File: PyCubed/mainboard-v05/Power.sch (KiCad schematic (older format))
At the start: 70 parts, among them J14 Conn_01x06, Q1 IRLML2803, Q2 MBT2222ADW1T1, Q22 NDS8434, Q3 MBT2222ADW1T1, U17 BQ25883RGER, U21 TPS7A4501DCQT, U4 ADM1176-1ARMZ-R7, U5 TPS54226PWPRPWP14_2P31X2P46-L, U6 LTC4121, U7 KF50BD-TR

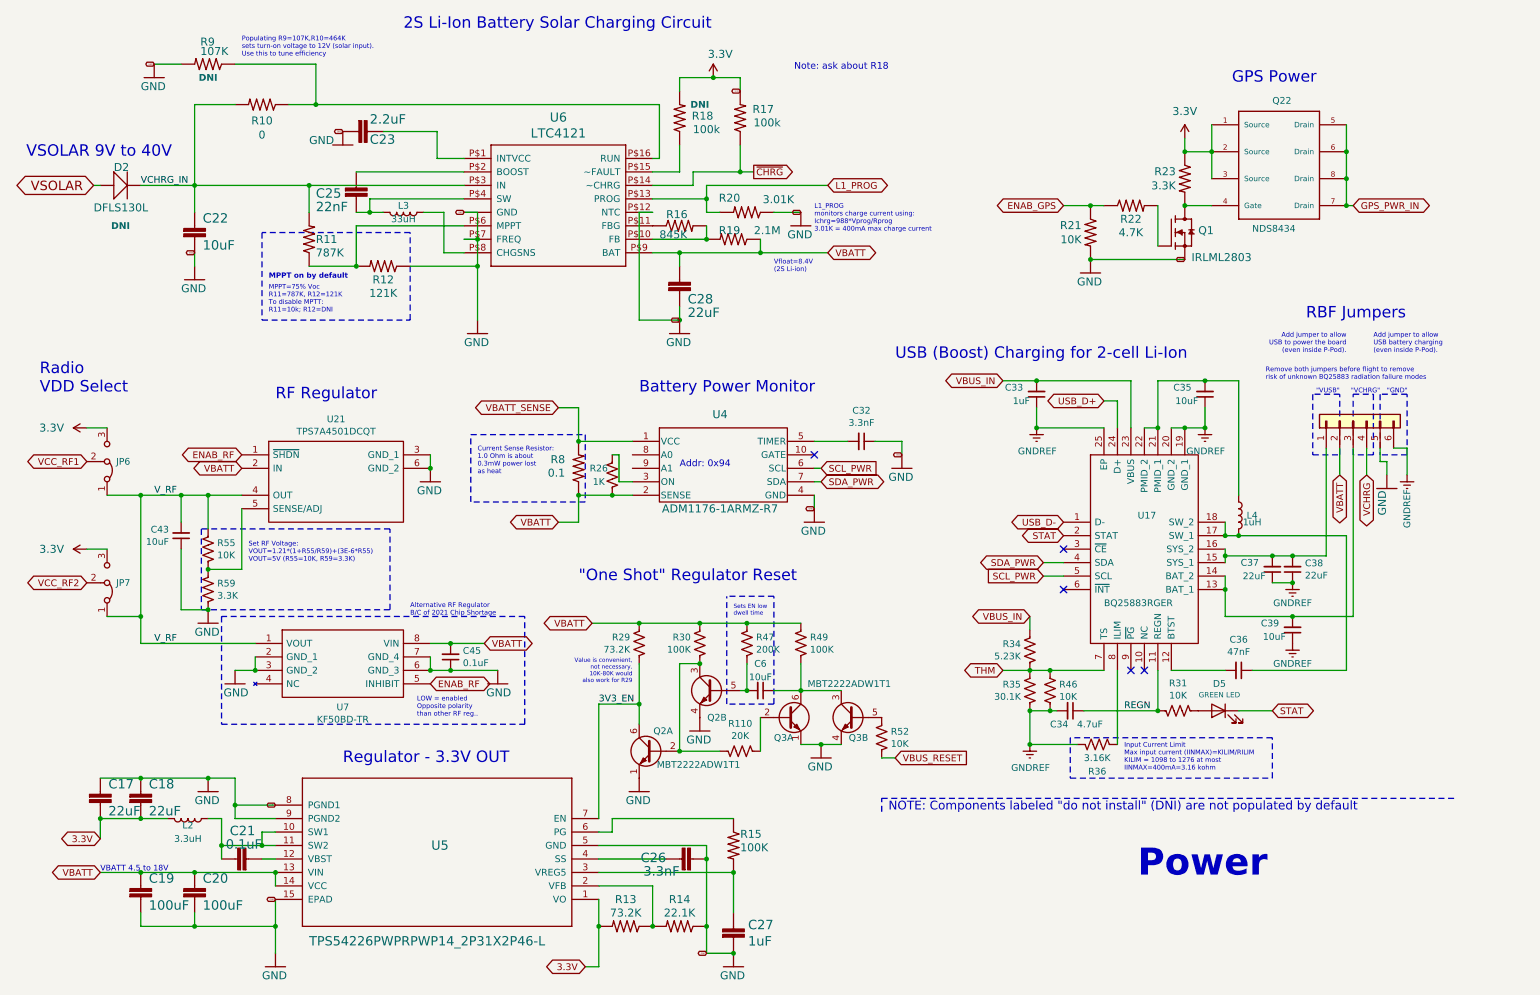
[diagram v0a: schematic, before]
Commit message: Battery board and side panels ready for CAD check and review, pycubed not finished yet
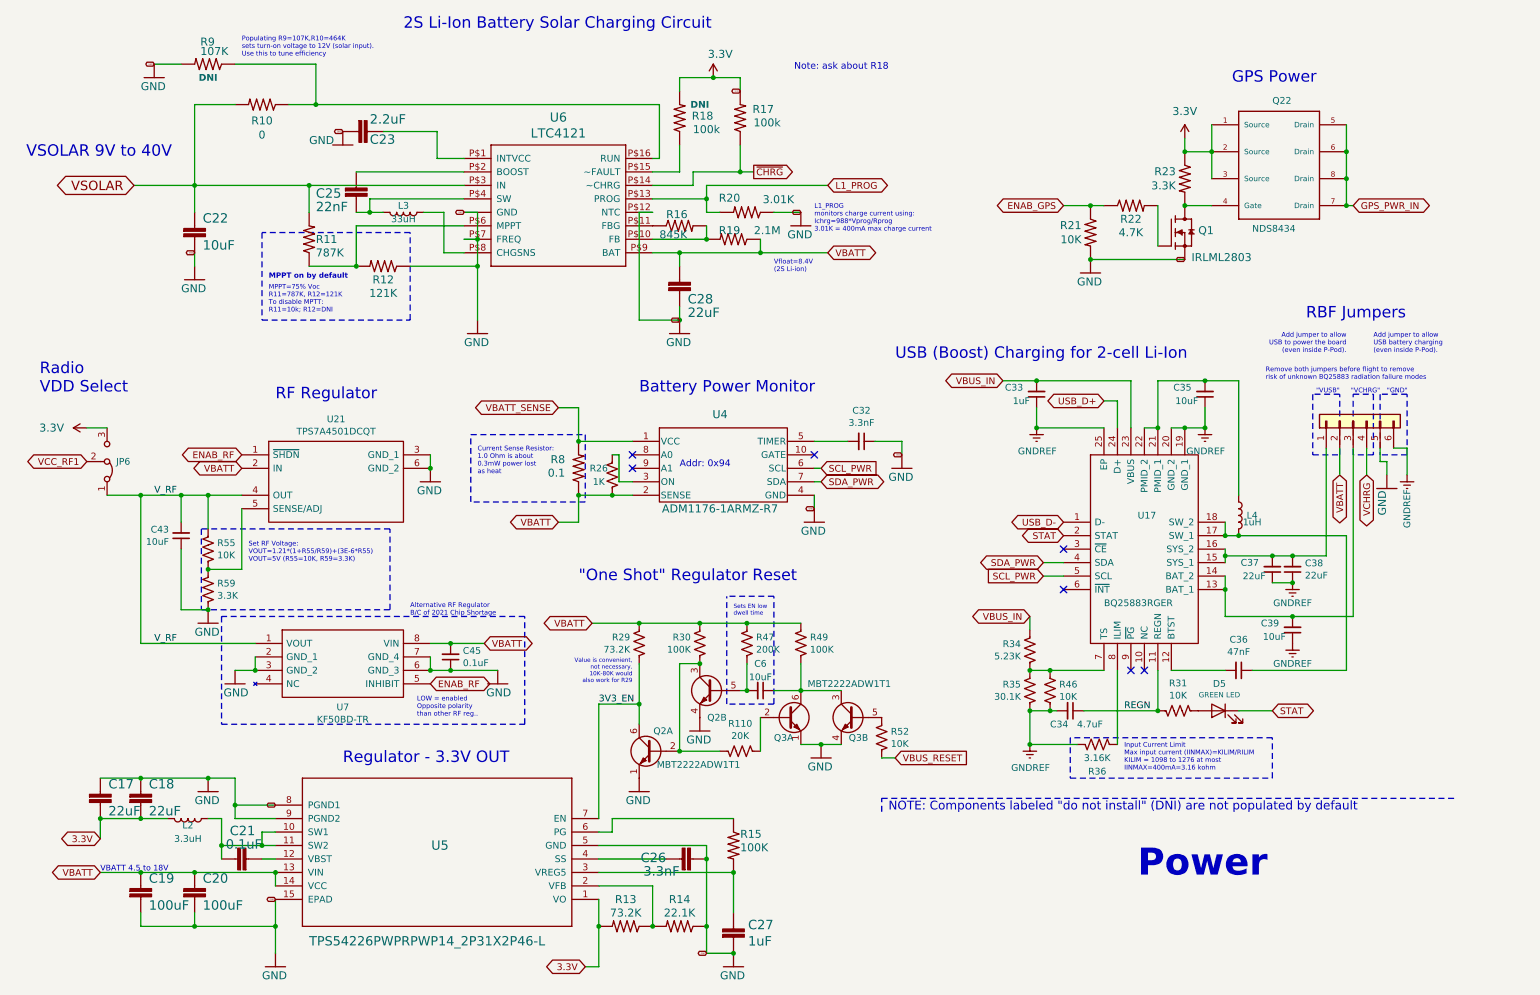
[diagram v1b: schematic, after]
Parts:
- removed D2: DFLS130L, mainboard:PWRDI-123, symbol mainboard:DFLS130L
- removed JP7: Jumper_3_Bridged12, mainboard:SolderJumper-3_P1.3mm_Bridged12_RoundedPad1.0x1.5mm, symbol Jumper:Jumper_3_Bridged12
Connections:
- net VCHRG_IN is gone; now on net VSOLAR: C22.1, R10.2, R11.2, U6.P$3 (IN)
- net THM: no longer names the net of R34.2, R35.2, R46.2, U17.7 (TS)
- no-connect marks 5 -> 7
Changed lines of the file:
@@
-$EndComp
-$Comp
-L mainboard:DFLS130L D?
-U 1 1 073F14D3
-P 1250 1850
-AR Path="/073F14D3" Ref="D?"  Part="1"
-AR Path="/5CEC5DDE/073F14D3" Ref="D2"  Part="1"
-F 0 "D2" H 1250 1950 59  0000 L BNN
-F 1 "DFLS130L" H 1100 1650 59  0000 L BNN
-F 2 "mainboard:PWRDI-123" H 1250 1850 50  0001 C CNN
-F 3 "https://www.diodes.com/assets/Datasheets/ds30492.pdf" H 1250 1850 50  0001 C CNN
-F 4 "Schottky Diode - 30V 1A" H 1250 1850 50  0001 C CNN "Description"
-F 5 "DFLS130L-7" H 1250 1850 50  0001 C CNN "Flight"
-F 6 "Diodes Incorporated" H 1250 1850 50  0001 C CNN "Manufacturer_Name"
-F 7 "DFLS130L-7" H 1250 2050 50  0001 C CNN "Manufacturer_Part_Number"
-F 8 "DFLS130L" H 1250 1850 50  0001 C CNN "Proto"
-F 9 "DNI" H 1300 1550 50  0000 C CNB "DNI"
-	1    1250 1850
-	1    0    0    -1
 $EndComp
 $Comp
@@
 $EndComp
 $Comp
-L mainboard:3.3V #SUPPLY?
-U 1 1 6090F0F5
-P 1050 4550
-AR Path="/6090F0F5" Ref="#SUPPLY?"  Part="1"
-AR Path="/5CEC6281/6090F0F5" Ref="#SUPPLY?"  Part="1"
-AR Path="/5CEC5DDE/6090F0F5" Ref="#SUPPLY0110"  Part="1"
-F 0 "#SUPPLY0110" H 1050 4550 50  0001 C CNN
-F 1 "3.3V" V 1050 4719 59  0000 L CNN
-F 2 "" H 1050 4550 50  0001 C CNN
-F 3 "" H 1050 4550 50  0001 C CNN
-	1    1050 4550
-	0    -1   -1   0
-$EndComp
-$Comp
 L Jumper:Jumper_3_Bridged12 JP6
 U 1 1 60AB2816
@@
 F 5 "Vertical Header - 0.1in (2.54mm)" H 1200 4067 50  0001 C CNN "Description"
 	1    1200 3900
-	0    1    -1   0
-$EndComp
-$Comp
-L Jumper:Jumper_3_Bridged12 JP7
-U 1 1 60B8D8AA
-P 1200 4800
-F 0 "JP7" V 1200 4867 50  0000 L CNN
-F 1 "Jumper_3_Bridged12" V 1245 4867 50  0001 L CNN
-F 2 "mainboard:SolderJumper-3_P1.3mm_Bridged12_RoundedPad1.0x1.5mm" H 1200 4800 50  0001 C CNN
-F 3 "" H 1200 4800 50  0001 C CNN
-F 4 "DNI" H 1200 4967 50  0001 C CNN "DNI"
-F 5 "Vertical Header - 0.1in (2.54mm)" H 1200 4967 50  0001 C CNN "Description"
-	1    1200 4800
 	0    1    -1   0
 $EndComp
@@
 Text GLabel 6000 1750 2    50   Output ~ 0
 ~CHRG
-Text GLabel 1100 1850 0    70   BiDi ~ 0
+Text GLabel 1400 1850 0    70   BiDi ~ 0
 VSOLAR
-Text Label 1450 1850 0    50   ~ 0
-VCHRG_IN
 Text Notes 7050 3150 0    85   ~ 0
 USB (Boost) Charging for 2-cell Li-Ion
@@
 Text GLabel 8050 5050 0    50   BiDi ~ 0
 VBUS_IN
-Text GLabel 7850 5450 0    50   BiDi ~ 0
-THM
 Text Notes 5450 3950 0    50   ~ 0
 Addr: 0x94
@@
 Text GLabel 1050 3900 0    50   BiDi ~ 0
 VCC_RF1
-Text GLabel 1050 4800 0    50   BiDi ~ 0
-VCC_RF2
 Wire Wire Line
 	1850 2350 1850 2450
@@
 	1450 6950 1850 6950
 Wire Wire Line
-	1150 1850 1100 1850
-Wire Wire Line
-	1450 1850 1850 1850
-Wire Wire Line
 	5150 2850 5450 2850
 Wire Wire Line
@@
 	8450 5750 9000 5750
 Wire Wire Line
-	8050 5450 7850 5450
-Wire Wire Line
 	3150 2050 3050 2050
 Wire Wire Line
@@
 	1750 5000 1950 5000
 Wire Wire Line
-	1450 5050 1450 4150
-Wire Wire Line
 	1450 4150 1750 4150
 Wire Wire Line
@@
 Wire Notes Line
 	3300 4400 1900 4400
-Wire Wire Line
-	1200 5050 1450 5050
-Wire Wire Line
-	1050 4550 1200 4550
 Wire Wire Line
 	1200 4150 1450 4150
@@
 	2300 5450 2300 5350
 Wire Wire Line
-	1450 5250 1450 5050
-Wire Wire Line
 	1450 5250 2300 5250
-Connection ~ 1450 5050
 Text GLabel 4000 5250 2    50   BiDi ~ 0
 VBATT
@@
 Text Notes 6300 1000 0    50   ~ 0
 Note: ask about R18
+Wire Wire Line
+	1450 4150 1450 5250
+NoConn ~ 5100 3850
+NoConn ~ 5100 3950
+Wire Wire Line
+	1400 1850 1850 1850
 $EndSCHEMATC
